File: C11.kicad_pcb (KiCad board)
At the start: 2 copper layers, 160.3 x 71.7 mm, 166 parts, among them IC1 MPM3610AGQV-P, IC2 THVD1450DRBR, IC3 THVD1450DRBR, IC4 THVD1450DRBR, IC5 THVD1450DRBR, IC6 MAX17613AATP+, IC8 MAX17613AATP+, J1 V24, J2 UDPI, J21 Conn_01x16, J22 RTBUS.out, J23 RTBUS.in, J3 Slot-0, J4 Slot-a1, J5 UDPI, J6 Screw_Terminal_01x04, J7 Slot-a0, J8 Screw_Terminal_01x02, J9 Conn_01x06, Q1 IRLML2060, U1 ATmega4809-M, U3 74AHC1G02, U4 74AHC1G02, U5 L78M12, U7 INA181A4, U9 ATmega4809-A, X1 ASE-24MHz

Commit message: Initial commit
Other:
- board text added: "RTB.base C11.4"
- board text added: "fschum '23"
- board text removed: "F.Schumacher'22"
- board text removed: "RTB.base C11.b"

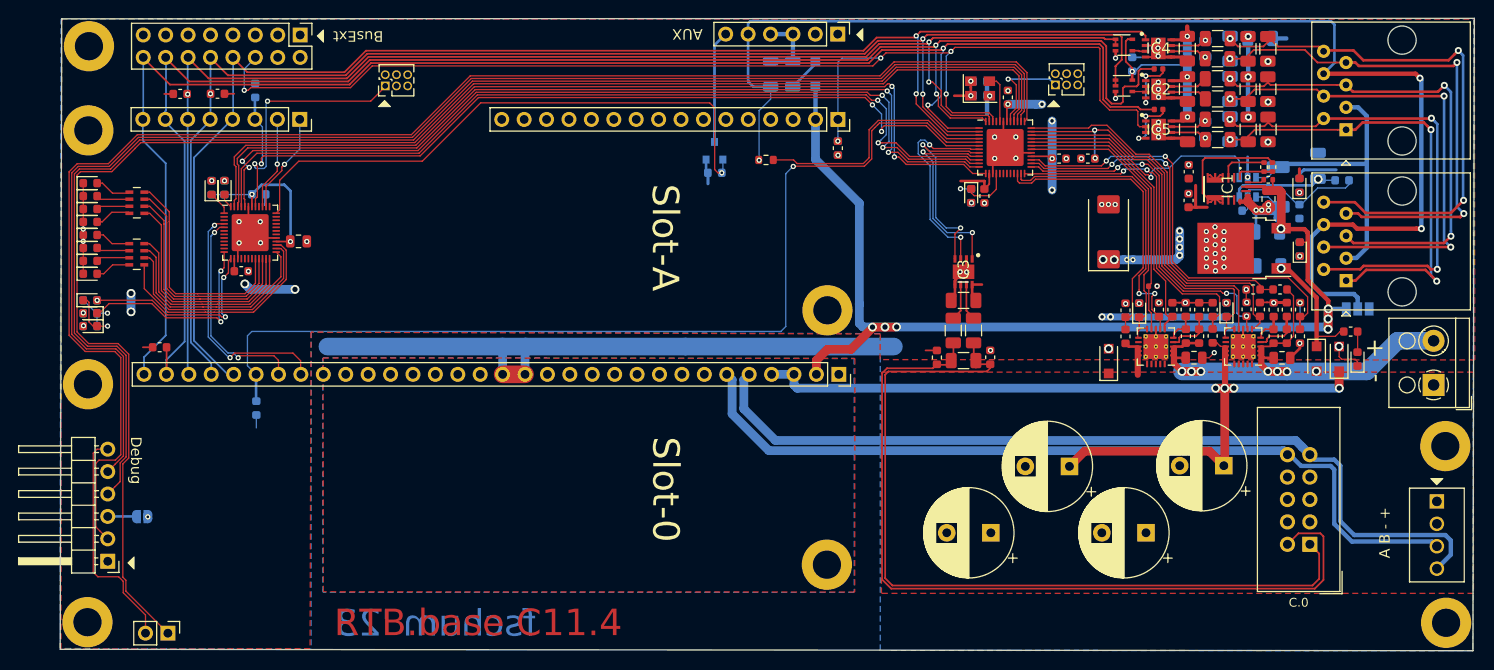
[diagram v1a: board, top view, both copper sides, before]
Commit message: mod: conversion to KiCad 9
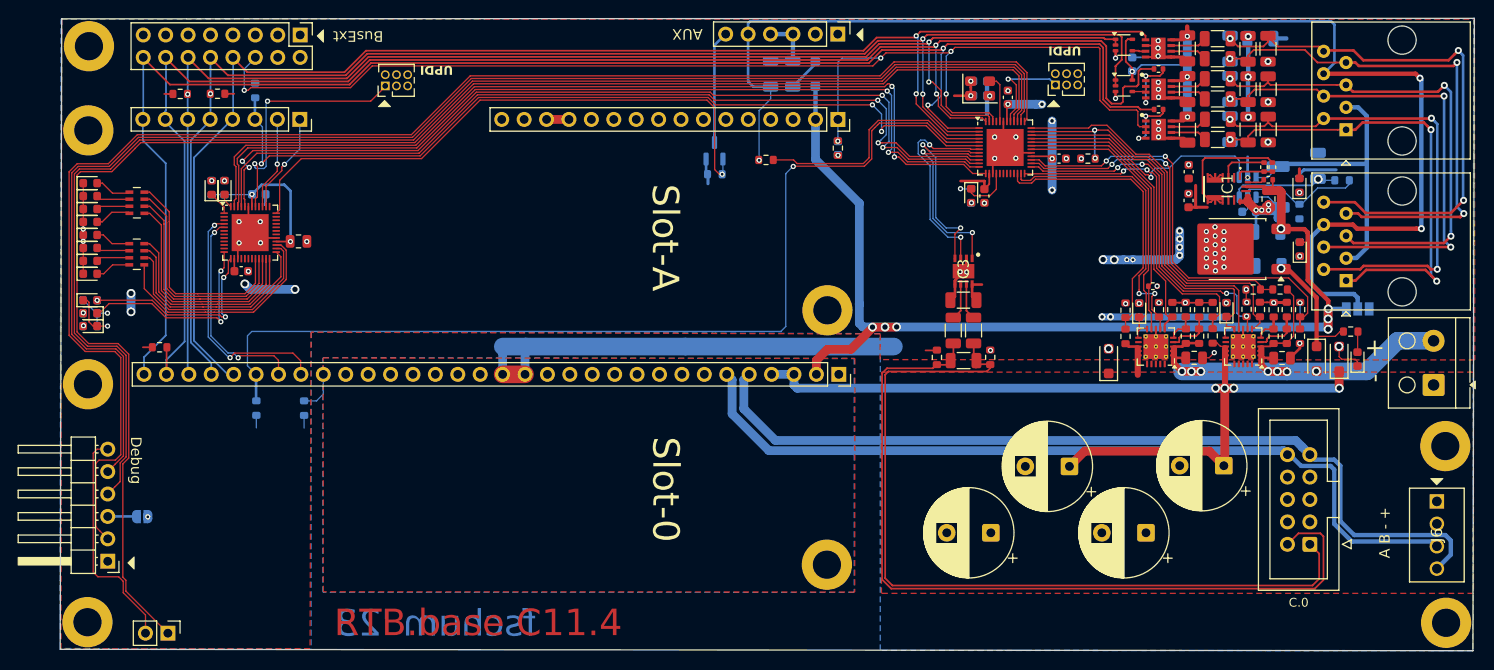
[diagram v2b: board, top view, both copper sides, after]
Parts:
- removed C11: 220u/25V, Capacitor_Tantalum_SMD:CP_EIA-7343-31_Kemet-D
- removed C29, C30: 4.7n, Capacitor_SMD:C_0805_2012Metric
- added R9: 10k, Resistor_SMD:R_0603_1608Metric, B.Cu at (77.7, -26.2)
- C13, C22, C5, C6: value 1u -> 100n
- C23, C4: value 1u -> 2.2u
- C26: value 4.7u/50V -> 4.7u
- C31: value 22u/25V -> 10u/16V
- D15: value LED_Small_ALT -> LED (wht)
- J1: value V24 -> V24 debug IF
- J6: footprint _Samac:1725672 -> RTB:1725672
- R1: value ? -> 100k
- R2: value ? -> 30.9k
- R29: value 5.1k -> 3.3k
- R47, R49: value 10k -> 3.3k
- R7, R8: value 390 -> 1k
- RN1: value 22k -> 4.7k
- U1: value ATmega4809-M -> AVR64DA48
- moved U5 0.85 mm to (183.3, -44.2)
- moved R55 0.16 mm to (124.2, -52.7)
- moved C22 0.13 mm to (184.8, -48.5)
- moved IC3 0.06 mm to (152.4, -41.7)
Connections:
- net ~BUS.bsi renamed ~{BUS.bsi}
- net ~BUS.bso renamed ~{BUS.bso}
- net ~BUS.rts renamed ~{BUS.rts}
- net ~RESET.0 renamed ~{RESET.0}
- net ~RESET.1 renamed ~{RESET.1}
- IC1 pad 10: (no net) -> unconnected-(IC1-NC_1-Pad10)
- IC1 pad 11: (no net) -> unconnected-(IC1-BST-Pad11)
- IC1 pad 15: (no net) -> unconnected-(IC1-NC_2-Pad15)
- IC1 pad 2: (no net) -> unconnected-(IC1-VCC-Pad2)
- IC6 pad 12: (no net) -> unconnected-(IC6-TSTART-Pad12)
- IC6 pad 14: (no net) -> Vbst.0
- IC6 pad 16: (no net) -> unconnected-(IC6-NC_1-Pad16)
- IC6 pad 17: (no net) -> unconnected-(IC6-NC_2-Pad17)
- IC6 pad 18: (no net) -> unconnected-(IC6-NC_3-Pad18)
- IC6 pad 19: (no net) -> unconnected-(IC6-NC_4-Pad19)
- IC6 pad 2: (no net) -> Vsrc
- IC6 pad 20: (no net) -> unconnected-(IC6-NC_5-Pad20)
- IC8 pad 12: (no net) -> unconnected-(IC8-TSTART-Pad12)
- IC8 pad 14: (no net) -> Vbst.1
- IC8 pad 16: (no net) -> unconnected-(IC8-NC_1-Pad16)
- IC8 pad 17: (no net) -> unconnected-(IC8-NC_2-Pad17)
- IC8 pad 18: (no net) -> unconnected-(IC8-NC_3-Pad18)
- IC8 pad 19: (no net) -> unconnected-(IC8-NC_4-Pad19)
- IC8 pad 2: (no net) -> Vsrc
- IC8 pad 20: (no net) -> unconnected-(IC8-NC_5-Pad20)
- J2 pad 3: (no net) -> unconnected-(J2-Pin_3-Pad3)
- J2 pad 4: (no net) -> unconnected-(J2-Pin_4-Pad4)
- J2 pad 5: (no net) -> unconnected-(J2-Pin_5-Pad5)
- J21 pad 1: (no net) -> unconnected-(J21-Pin_1-Pad1)
- J21 pad 2: (no net) -> unconnected-(J21-Pin_2-Pad2)
- J3 pad 1: (no net) -> unconnected-(J3-Pin_1-Pad1)
- J3 pad 10: (no net) -> unconnected-(J3-Pin_10-Pad10)
- J3 pad 11: (no net) -> unconnected-(J3-Pin_11-Pad11)
- J3 pad 12: (no net) -> unconnected-(J3-Pin_12-Pad12)
- J3 pad 13: (no net) -> unconnected-(J3-Pin_13-Pad13)
- J3 pad 14: (no net) -> unconnected-(J3-Pin_14-Pad14)
- J3 pad 17: (no net) -> unconnected-(J3-Pin_17-Pad17)
- J3 pad 18: (no net) -> unconnected-(J3-Pin_18-Pad18)
- J3 pad 19: (no net) -> unconnected-(J3-Pin_19-Pad19)
- J3 pad 20: (no net) -> unconnected-(J3-Pin_20-Pad20)
- J3 pad 21: (no net) -> unconnected-(J3-Pin_21-Pad21)
- J3 pad 22: (no net) -> unconnected-(J3-Pin_22-Pad22)
- J3 pad 23: (no net) -> unconnected-(J3-Pin_23-Pad23)
- J3 pad 24: (no net) -> Net-(J3-Pin_24)
- J3 pad 7: (no net) -> unconnected-(J3-Pin_7-Pad7)
- J3 pad 8: (no net) -> unconnected-(J3-Pin_8-Pad8)
- J3 pad 9: (no net) -> unconnected-(J3-Pin_9-Pad9)
- J5 pad 3: (no net) -> unconnected-(J5-Pin_3-Pad3)
- J5 pad 4: (no net) -> unconnected-(J5-Pin_4-Pad4)
- J5 pad 5: (no net) -> unconnected-(J5-Pin_5-Pad5)
- J7 pad 10: (no net) -> unconnected-(J7-Pin_10-Pad10)
- J7 pad 11: (no net) -> unconnected-(J7-Pin_11-Pad11)
- J7 pad 12: (no net) -> unconnected-(J7-Pin_12-Pad12)
- J7 pad 13: (no net) -> VBUS
- J7 pad 14: (no net) -> VBUS
- J7 pad 3: (no net) -> unconnected-(J7-Pin_3-Pad3)
- J7 pad 4: (no net) -> unconnected-(J7-Pin_4-Pad4)
- J7 pad 5: (no net) -> unconnected-(J7-Pin_5-Pad5)
- J7 pad 6: (no net) -> unconnected-(J7-Pin_6-Pad6)
- J7 pad 7: (no net) -> unconnected-(J7-Pin_7-Pad7)
- J7 pad 8: (no net) -> unconnected-(J7-Pin_8-Pad8)
- J7 pad 9: (no net) -> unconnected-(J7-Pin_9-Pad9)
- U1 pad 17: (no net) -> unconnected-(U1-PC5-Pad17)
- U1 pad 18: (no net) -> unconnected-(U1-PC6-Pad18)
- U1 pad 19: (no net) -> unconnected-(U1-PC7-Pad19)
- U1 pad 20: (no net) -> unconnected-(U1-PD0-Pad20)
- U1 pad 21: (no net) -> unconnected-(U1-PD1-Pad21)
- U1 pad 45: (no net) -> unconnected-(U1-PA1-Pad45)
- U1 pad 49: (no net) -> GND
- U9 pad 10: (no net) -> SLT2.rx
- U9 pad 11: (no net) -> SLT2.tx
- U9 pad 16: (no net) -> unconnected-(U9-PC4-Pad16)
- U9 pad 17: (no net) -> unconnected-(U9-PC5-Pad17)
- U9 pad 18: (no net) -> unconnected-(U9-PC6-Pad18)
- U9 pad 19: (no net) -> unconnected-(U9-PC7-Pad19)
- U9 pad 2: (no net) -> unconnected-(U9-PA6-Pad2)
- U9 pad 3: (no net) -> unconnected-(U9-PA7-Pad3)
- U9 pad 30: (no net) -> MOSI
- U9 pad 31: (no net) -> MISO
- U9 pad 32: (no net) -> SCK
- U9 pad 33: (no net) -> SS_bme
- U9 pad 34: (no net) -> SS_bmi
- U9 pad 35: (no net) -> IRQ_bmi
- U9 pad 37: (no net) -> unconnected-(U9-PF3-Pad37)
- U9 pad 40: (no net) -> ~{RESET.cex}
- U9 pad 49: (no net) -> GND
- U9 pad 6: (no net) -> unconnected-(U9-PB2-Pad6)
- U9 pad 7: (no net) -> unconnected-(U9-PB3-Pad7)
- U9 pad 8: (no net) -> unconnected-(U9-PB4-Pad8)
- U9 pad 9: (no net) -> unconnected-(U9-PB5-Pad9)
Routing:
- net GND: track 188.6 -> 170.2 mm, vias 73 -> 70
- net Net-(J3-Pin_24): track 0.00 -> 4.73 mm
- net VBUS: track 0.00 -> 2.54 mm
- net OUT.1: track 66.6 -> 67.1 mm
- net Net-(IC5-B): vias 1 -> 0
- net Net-(IC5-A): vias 1 -> 0
- net Net-(IC4-B): vias 1 -> 0
- net Net-(IC4-A): vias 1 -> 0
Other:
- net class Default removed
- net class Power removed
- board text added: "UPDI"

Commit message: mod: changed to buck converter
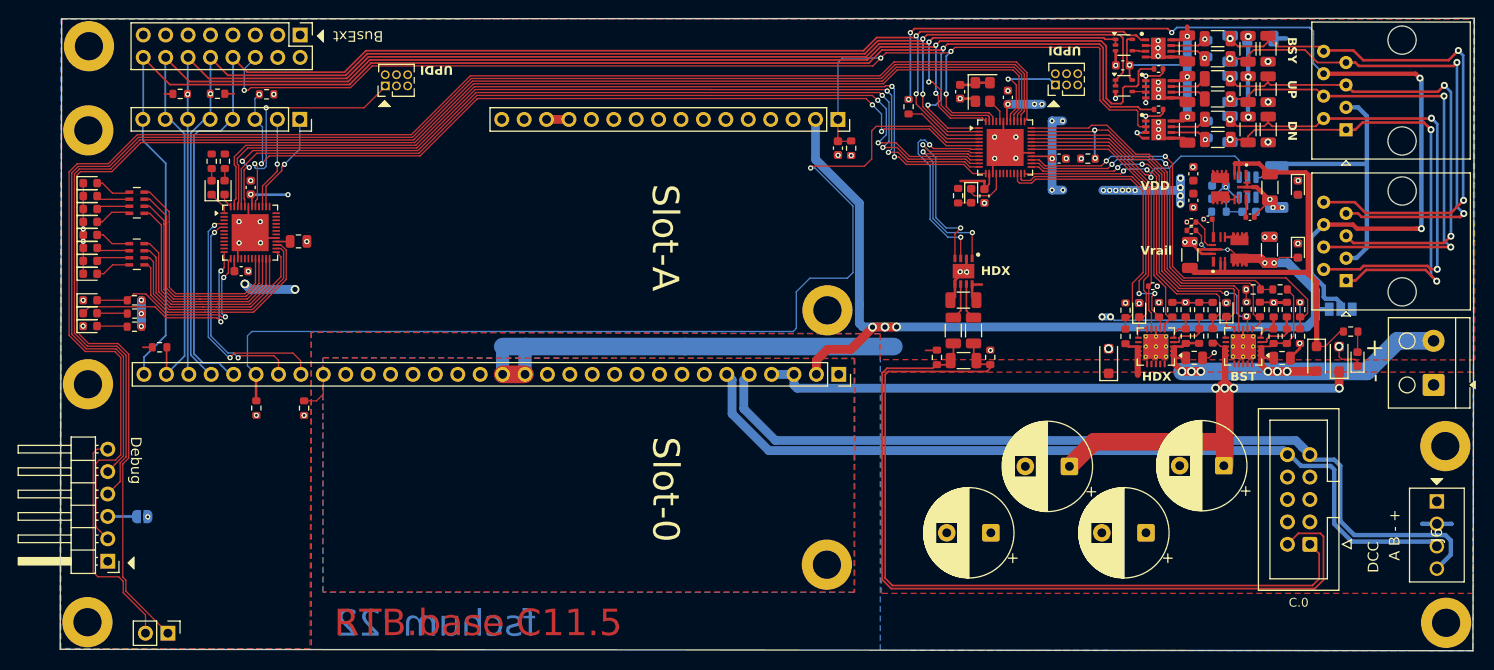
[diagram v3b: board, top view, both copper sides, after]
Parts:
- removed D23: D, Diode_SMD:D_SOD-123F
- removed J9: Conn_01x06, Connector_PinHeader_2.54mm:PinHeader_1x06_P2.54mm_Vertical
- removed Q1: IRLML2060, Package_TO_SOT_SMD:SOT-23
- removed R3: 100k, Resistor_SMD:R_0402_1005Metric
- removed R5: 1k, Resistor_SMD:R_1206_3216Metric
- removed R55: 100k, Resistor_SMD:R_0603_1608Metric
- removed R6: 120, Resistor_SMD:R_1206_3216Metric
- removed U5: L78M12, Package_TO_SOT_SMD:TO-252-2
- added C11: 10u, Capacitor_SMD:C_1206_3216Metric, B.Cu at (187.1, -44.1)
- added C29: 4.7n, Capacitor_SMD:C_0805_2012Metric, B.Cu at (179.9, -57.8)
- added C30: 4.7n, Capacitor_SMD:C_0805_2012Metric, B.Cu at (179.9, -67.0)
- added C32: 1u, Capacitor_SMD:C_0402_1005Metric, F.Cu at (180.1, -47.6)
- added IC7: TPSM365R15RDNR, RTB:TPSM365R3RDNR, F.Cu at (182.5, -51.3)
- C10: value 10u/25V -> 2.2u/50V; footprint Capacitor_SMD:C_0805_2012Metric -> Capacitor_SMD:C_1206_3216Metric
- C12, C31: value 10u/16V -> 10u/25V
- C2, C7, C8, C9: value 2.2u -> 2.2u/50V
- C23: footprint Capacitor_SMD:C_1206_3216Metric -> Capacitor_SMD:C_0603_1608Metric
- C24, C28, C3, R29, R43, R45, R46, R50, R80, R81, R9: moved to F.Cu
- C25: value 220n -> 100n; moved to F.Cu
- C26: value 4.7u -> 10u; moved to F.Cu
- C27: value 4.7u/50V -> 2.2u/50V; moved to F.Cu
- C4: value 2.2u -> 1u; footprint Capacitor_SMD:C_0603_1608Metric -> Capacitor_SMD:C_0402_1005Metric; moved to F.Cu
- D1, D5, D9: value D -> SSA34
- IC1: value MPM3610AGQV-P -> TPSM365R15RDNR; footprint RTB:MPM3610AGQVP -> RTB:TPSM365R3RDNR
- R2: value 30.9k -> 9.1k
- R22, R37: value 47k -> 42.2k
- R72: value 2.2k -> 3.3k; moved to F.Cu
- U7: value INA181A4 -> INA181A1
- moved C4 34.3 mm to (184.9, -47.9), turned to 0 degrees
- moved R4 17.2 mm to (146.2, -60.4), turned to 90 degrees
- moved R83 14.1 mm to (181.3, -50.0)
- moved R1 11.7 mm to (178.2, -46.4), turned to 0 degrees
- moved C23 11.4 mm to (181.3, -51.4), turned to 180 degrees
- moved R2 10.3 mm to (178.2, -47.3), turned to 0 degrees
- moved R82 9.12 mm to (181.3, -48.5), turned to 180 degrees
- moved C27 9.00 mm to (178.1, -43.6), turned to -90 degrees
- moved IC1 6.88 mm to (182.7, -44.2), turned to 90 degrees
- moved R80 5.04 mm to (58.5, -36.9)
- moved R81 5.04 mm to (58.5, -38.4), turned to 180 degrees
- moved R72 5.03 mm to (58.5, -35.4)
- moved R46 2.99 mm to (68.7, -54.2), turned to 90 degrees
- moved R50 2.99 mm to (67.2, -54.2), turned to 90 degrees
- moved C3 2.30 mm to (152.0, -62.1), turned to 90 degrees
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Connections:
- C10 pad 1: GND -> Vpos
- C10 pad 2: Vrail -> GND
- C27 pad 1: Net-(D1-K) -> GND
- C27 pad 2: GND -> Vpos
- C4 pad 1: GND -> Net-(IC7-VCC)
- C4 pad 2: +3V3 -> GND
- D1 pad 1: Net-(D1-K) -> Vpos
- IC1 pad 1: Net-(IC1-FB) -> unconnected-(IC1-PGOOD-Pad1)
- IC1 pad 10: unconnected-(IC1-NC_1-Pad10) -> GND
- IC1 pad 11: unconnected-(IC1-BST-Pad11) -> GND
- IC1 pad 12: GND -> Vrail
- IC1 pad 13: GND -> Vrail
- IC1 pad 14: GND -> Vrail
- IC1 pad 15: unconnected-(IC1-NC_2-Pad15) -> Vrail
- IC1 pad 16: Vrail -> Net-(IC1-SW_1_1)
- IC1 pad 17: Net-(IC1-EN) -> Net-(IC1-SW_1_1)
- IC1 pad 18: GND -> Net-(IC1-SW_1_1)
- IC1 pad 19: Net-(IC1-SW_1) -> Net-(IC1-SW_1_1)
- IC1 pad 2: unconnected-(IC1-VCC-Pad2) -> Vpos
- IC1 pad 3: Net-(IC1-AGND) -> Vpos
- IC1 pad 4: Net-(IC1-SW_1) -> Vrail
- IC1 pad 5: Net-(IC1-SW_1) -> Net-(IC1-SW_1_1)
- IC1 pad 6: Net-(IC1-SW_1) -> Net-(IC1-SW_1_1)
- IC1 pad 7: +3V3 -> unconnected-(IC1-BOOT-Pad7)
- IC1 pad 8: +3V3 -> Net-(IC1-VCC)
- IC1 pad 9: +3V3 -> Net-(IC1-FB/BIAS)
- R1 pad 1: +3V3 -> Net-(IC1-FB/BIAS)
- R1 pad 2: Net-(IC1-FB) -> Vrail
- R2 pad 1: Net-(IC1-FB) -> GND
- R2 pad 2: Net-(IC1-AGND) -> Net-(IC1-FB/BIAS)
- R89 pad 2: Net-(D1-K) -> Vpos
- U9 pad 36: OUT.1 -> unconnected-(U9-PF2-Pad36)
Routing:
- net OUT.1: track 67.1 -> 0.00 mm, vias 1 -> 0
- net Vpos: track 0.00 -> 55.3 mm
- net +3V3: track 168.2 -> 130.9 mm, vias 34 -> 36
- net BUS.opt: track 145.0 -> 111.2 mm, vias 3 -> 5
- net Net-(U1-PB0): track 28.2 -> 9.15 mm
- net GND: track 170.2 -> 153.1 mm, vias 70 -> 64
- net Net-(D1-K): track 14.1 -> 0.00 mm, vias 1 -> 0
- net Net-(J9-Pin_6): track 12.8 -> 0.00 mm
- net Net-(U7-REF): track 16.4 -> 5.32 mm
- net Net-(J9-Pin_3): track 8.09 -> 0.00 mm
- net Vrail: track 127.8 -> 121.1 mm
- net ~{RESET.1}: track 113.6 -> 119.6 mm
- net Net-(IC1-SW_1_1): track 0.00 -> 5.62 mm
- net Net-(IC7-SW_1_1): track 0.00 -> 5.62 mm
- net Net-(IC1-AGND): track 5.56 -> 0.00 mm
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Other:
- rule pad_to_mask_clearance: 0.2 -> 0
- board text added: "BST"
- board text added: "BSY"
- board text added: "DCC"
- board text added: "DN"
- board text added: "HDX"
- board text added: "RTB.base C11.5"
- board text added: "UP"
- board text added: "VDD"
- board text added: "Vrail"
- board text added: "fschum '22"
- board text removed: "AUX"
- board text removed: "RTB.base C11.4"
- board text removed: "fschum '23"

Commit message: refined BOM
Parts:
- added C33: 100n, Capacitor_SMD:C_0603_1608Metric, B.Cu at (181.4, -52.9)
- added R3: 10k, Resistor_SMD:R_0603_1608Metric, B.Cu at (181.4, -54.4)
- C1, C15, C17, C18: value 220u/25V -> 470u/25V
- U3, U4: footprint Package_TO_SOT_SMD:SOT-353_SC-70-5 -> RTB:SOT65P210X110-5N
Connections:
- U7 pad 1: ADC.gnd -> Net-(R3-Pad2)
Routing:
- net Net-(R3-Pad2): track 0.00 -> 3.35 mm
- net ADC.gnd: track 28.9 -> 26.2 mm
